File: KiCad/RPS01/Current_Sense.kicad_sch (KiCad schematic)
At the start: 8 parts, among them U7 INA139NA/250

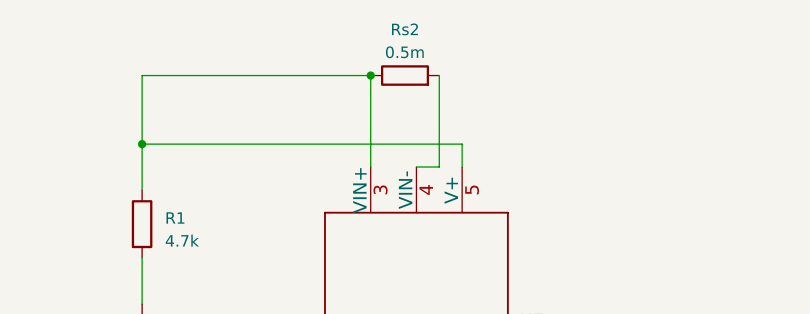
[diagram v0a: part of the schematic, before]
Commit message: 19V Update
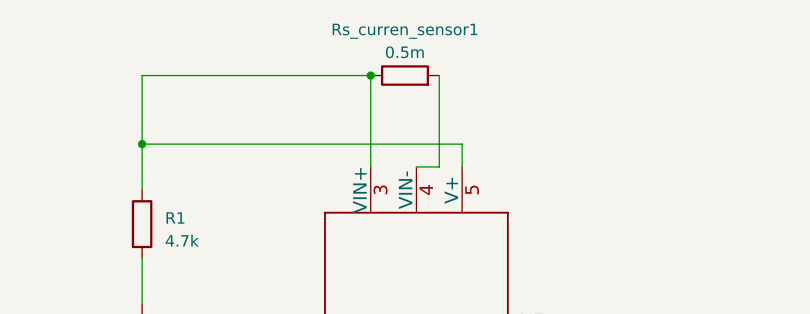
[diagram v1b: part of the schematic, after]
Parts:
- renumbered Rs2 to Rs_curren_sensor1
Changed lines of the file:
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@@
   (symbol (lib_id "Device:R") (at 62.23 38.1 90) (unit 1)
     (in_bom yes) (on_board yes) (dnp no) (fields_autoplaced)
-    (property "Reference" "Rs2" (at 62.23 33.02 90)
+    (property "Reference" "Rs_curren_sensor1" (at 62.23 33.02 90)
       (effects (font (size 1.27 1.27)))
     )
@@
       (project "rps01"
         (path "/14930f15-c0a0-4b55-93e6-b112548415f6/13e150ee-6c46-47a5-9c09-3749eb0dcbfe"
-          (reference "Rs2") (unit 1)
+          (reference "Rs_curren_sensor1") (unit 1)
         )
       )

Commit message: Deleted Current Sense Circuit to remove errors and started 5V system
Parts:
- removed C1, C2: 0.1mu, Capacitor_SMD:C_1206_3216Metric, symbol Device:C
- removed R1: 4.7k, Resistor_SMD:R_1206_3216Metric, symbol Device:R
- removed R2: 10k, Resistor_SMD:R_1206_3216Metric, symbol Device:R
- removed R3: 1k, Resistor_SMD:R_1206_3216Metric, symbol Device:R
- removed RL1: 72.3k, Resistor_SMD:R_1210_3225Metric, symbol Device:R
- removed Rs_curren_sensor1: 0.5m, Resistor_SMD:R_1206_3216Metric, symbol Device:R
- removed U7: INA139NA/250, Mechatronic Footprints:INA139_PW8, symbol 2023-04-06_06-18-16:INA139NA/250

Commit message: Add Current Sense to RPS01
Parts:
- added R1: 0.3m, symbol Device:R
- added U12: INA139QPWRQ1, PW8, symbol INA139:INA139QPWRQ1
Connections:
- new net +5V: U12.8 (V-)
- new net GND: U12.4 (GND)
- new net Load: R1.2, U12.1 (VIN-)
- new net SenseVoltage: U12.6 (OUT)
- new net Vp: R1.1, U12.2 (VIN+)
- no-connect marks 0 -> 3
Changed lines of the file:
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@@
 (kicad_sch (version 20230121) (generator eeschema)
   (paper "A4")
-  (image (at 123.19 160.528) (scale 1.22369)
+  (junction (at 104.14 35.56) (diameter 0) (color 0 0 0 0)
+  )
+  (junction (at 113.6342 35.56) (diameter 0) (color 0 0 0 0)
+  )
+  (no_connect (at 101.6 97.79))
+  (no_connect (at 104.14 41.91))
+  (no_connect (at 106.68 97.79))
+  (wire (pts (xy 105.41 35.56) (xy 104.14 35.56))
+    (stroke (width 0) (type default))
+  )
+  (wire (pts (xy 85.09 35.56) (xy 104.14 35.56))
+    (stroke (width 0) (type default))
+  )
+  (wire (pts (xy 101.6 41.91) (xy 81.28 41.91))
+    (stroke (width 0) (type default))
+  )
+  (wire (pts (xy 109.22 97.79) (xy 123.19 97.79))
+    (stroke (width 0) (type default))
+  )
+  (wire (pts (xy 113.6342 35.56) (xy 139.7 35.56))
+    (stroke (width 0) (type default))
+  )
+  (wire (pts (xy 113.6342 41.91) (xy 109.22 41.91))
+    (stroke (width 0) (type default))
+  )
+  (wire (pts (xy 104.14 97.79) (xy 104.14 101.6))
+    (stroke (width 0) (type default))
+  )
+  (wire (pts (xy 113.6342 35.56) (xy 113.6342 41.91))
+    (stroke (width 0) (type default))
+  )
+  (wire (pts (xy 113.03 35.56) (xy 113.6342 35.56))
+    (stroke (width 0) (type default))
+  )
+  (wire (pts (xy 81.28 41.91) (xy 81.28 53.34))
+    (stroke (width 0) (type default))
+  )
+  (wire (pts (xy 104.14 101.6) (xy 133.35 101.6))
+    (stroke (width 0) (type default))
+  )
+  (wire (pts (xy 104.14 38.3106) (xy 104.14 35.56))
+    (stroke (width 0) (type default))
+  )
+  (wire (pts (xy 106.68 41.91) (xy 106.68 38.3106))
+    (stroke (width 0) (type default))
+  )
+  (wire (pts (xy 106.68 38.3106) (xy 104.14 38.3106))
+    (stroke (width 0) (type default))
+  )
+  (image (at 120.65 142.748) (scale 1.22369)
     (data
       iVBORw0KGgoAAAANSUhEUgAAA2QAAAJMCAIAAAAaAvJwAAAAA3NCSVQICAjb4U/gAAAACXBIWXMA
@@
     )
   )
-  (image (at 197.612 70.358) (scale 1.93163)
+  (image (at 231.902 47.498) (scale 1.16665)
     (data
       iVBORw0KGgoAAAANSUhEUgAABAIAAAKsCAIAAAD5hIhGAAAAA3NCSVQICAjb4U/gAAAACXBIWXMA
@@
     )
   )
+  (hierarchical_label "Load" (shape input) (at 139.7 35.56 0) (fields_autoplaced)
+    (effects (font (size 1.27 1.27)) (justify left))
+  )
+  (hierarchical_label "SenseVoltage" (shape input) (at 133.35 101.6 0) (fields_autoplaced)
+    (effects (font (size 1.27 1.27)) (justify left))
+  )
+  (hierarchical_label "Vp" (shape input) (at 85.09 35.56 180) (fields_autoplaced)
+    (effects (font (size 1.27 1.27)) (justify right))
+  )
+  (symbol (lib_id "power:GND") (at 81.28 53.34 0) (unit 1)
+    (in_bom yes) (on_board yes) (dnp no) (fields_autoplaced)
+    (property "Reference" "#PWR030" (at 81.28 59.69 0)
+      (effects (font (size 1.27 1.27)) hide)
+    )
+    (property "Value" "GND" (at 81.28 58.42 0)
+      (effects (font (size 1.27 1.27)))
+    )
+    (property "Footprint" "" (at 81.28 53.34 0)
+      (effects (font (size 1.27 1.27)) hide)
+    )
+    (property "Datasheet" "" (at 81.28 53.34 0)
+      (effects (font (size 1.27 1.27)) hide)
+    )
+    (pin "1")
+    (instances
+      (project "rps01"
+        (path "/14930f15-c0a0-4b55-93e6-b112548415f6/13e150ee-6c46-47a5-9c09-3749eb0dcbfe"
+          (reference "#PWR030") (unit 1)
+        )
+      )
+    )
+  )
+  (symbol (lib_id "Device:R") (at 109.22 35.56 90) (unit 1)
+    (in_bom yes) (on_board yes) (dnp no) (fields_autoplaced)
+    (property "Reference" "R1" (at 109.22 30.48 90)
+      (effects (font (size 1.27 1.27)))
+    )
+    (property "Value" "0.3m" (at 109.22 33.02 90)
+      (effects (font (size 1.27 1.27)))
+    )
+    (property "Footprint" "" (at 109.22 37.338 90)
+      (effects (font (size 1.27 1.27)) hide)
+    )
+    (property "Datasheet" "~" (at 109.22 35.56 0)
+      (effects (font (size 1.27 1.27)) hide)
+    )
+    (pin "1")
+    (pin "2")
+    (instances
+      (project "rps01"
+        (path "/14930f15-c0a0-4b55-93e6-b112548415f6/13e150ee-6c46-47a5-9c09-3749eb0dcbfe"
+          (reference "R1") (unit 1)
+        )
+      )
+    )
+  )
+  (symbol (lib_id "power:+5V") (at 123.19 97.79 270) (unit 1)
+    (in_bom yes) (on_board yes) (dnp no) (fields_autoplaced)
+    (property "Reference" "#PWR031" (at 119.38 97.79 0)
+      (effects (font (size 1.27 1.27)) hide)
+    )
+    (property "Value" "+5V" (at 127 98.425 90)
+      (effects (font (size 1.27 1.27)) (justify left))
+    )
+    (property "Footprint" "" (at 123.19 97.79 0)
+      (effects (font (size 1.27 1.27)) hide)
+    )
+    (property "Datasheet" "" (at 123.19 97.79 0)
+      (effects (font (size 1.27 1.27)) hide)
+    )
+    (pin "1")
+    (instances
+      (project "rps01"
+        (path "/14930f15-c0a0-4b55-93e6-b112548415f6/13e150ee-6c46-47a5-9c09-3749eb0dcbfe"
+          (reference "#PWR031") (unit 1)
+        )
+      )
+    )
+  )
+  (symbol (lib_id "INA139:INA139QPWRQ1") (at 109.22 41.91 270) (unit 1)
+    (in_bom yes) (on_board yes) (dnp no) (fields_autoplaced)
+    (property "Reference" "U12" (at 115.57 69.215 90)
+      (effects (font (size 1.524 1.524)) (justify left))
+    )
+    (property "Value" "INA139QPWRQ1" (at 115.57 71.755 90)
+      (effects (font (size 1.524 1.524)) (justify left))
+    )
+    (property "Footprint" "PW8" (at 109.22 41.91 0)
+      (effects (font (size 1.27 1.27) italic) hide)
+    )
+    (property "Datasheet" "INA139QPWRQ1" (at 109.22 41.91 0)
+      (effects (font (size 1.27 1.27) italic) hide)
+    )
+    (pin "1")
+    (pin "2")
+    (pin "3")
+    (pin "4")
+    (pin "5")
+    (pin "6")
+    (pin "7")
+    (pin "8")
+    (instances
+      (project "rps01"
+        (path "/14930f15-c0a0-4b55-93e6-b112548415f6/13e150ee-6c46-47a5-9c09-3749eb0dcbfe"
+          (reference "U12") (unit 1)
+        )
+      )
+    )
+  )

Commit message: Add Fuses and other ADC pin
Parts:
- R1: footprint (none) -> Mechatronic Footprints:CSS2H-5930R
- U12: footprint PW8 -> Mechatronic Footprints:INA139_PW8
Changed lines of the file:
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@@
       (effects (font (size 1.27 1.27)))
     )
-    (property "Footprint" "" (at 109.22 37.338 90)
+    (property "Footprint" "Mechatronic Footprints:CSS2H-5930R" (at 109.22 37.338 90)
       (effects (font (size 1.27 1.27)) hide)
     )
@@
       (effects (font (size 1.524 1.524)) (justify left))
     )
-    (property "Footprint" "PW8" (at 109.22 41.91 0)
+    (property "Footprint" "Mechatronic Footprints:INA139_PW8" (at 109.22 41.91 0)
       (effects (font (size 1.27 1.27) italic) hide)
     )

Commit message: adjustments to main board revision
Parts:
- added Cf_1: 80pF, symbol Device:C
- added RL: 100k, symbol Device:R
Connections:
- net GND: now also Cf_1.2, RL.1
- net SenseVoltage: now also Cf_1.1, RL.2
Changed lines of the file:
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@@
   (junction (at 104.14 35.56) (diameter 0) (color 0 0 0 0)
   )
+  (junction (at 111.76 117.3986) (diameter 0) (color 0 0 0 0)
+  )
   (junction (at 113.6342 35.56) (diameter 0) (color 0 0 0 0)
   )
+  (junction (at 121.92 101.6158) (diameter 0) (color 0 0 0 0)
+  )
+  (junction (at 111.76 101.6158) (diameter 0) (color 0 0 0 0)
+  )
   (no_connect (at 101.6 97.79))
   (no_connect (at 104.14 41.91))
   (no_connect (at 106.68 97.79))
+  (wire (pts (xy 121.92 101.6158) (xy 133.35 101.6158))
+    (stroke (width 0) (type default))
+  )
   (wire (pts (xy 105.41 35.56) (xy 104.14 35.56))
     (stroke (width 0) (type default))
   )
+  (wire (pts (xy 121.92 113.03) (xy 121.92 117.3986))
+    (stroke (width 0) (type default))
+  )
+  (wire (pts (xy 111.76 101.6158) (xy 111.76 105.41))
+    (stroke (width 0) (type default))
+  )
   (wire (pts (xy 85.09 35.56) (xy 104.14 35.56))
     (stroke (width 0) (type default))
   )
+  (wire (pts (xy 121.92 117.3986) (xy 111.76 117.3986))
+    (stroke (width 0) (type default))
+  )
   (wire (pts (xy 101.6 41.91) (xy 81.28 41.91))
     (stroke (width 0) (type default))
   )
+  (wire (pts (xy 111.76 117.3986) (xy 111.76 119.38))
+    (stroke (width 0) (type default))
+  )
   (wire (pts (xy 109.22 97.79) (xy 123.19 97.79))
     (stroke (width 0) (type default))
   )
+  (wire (pts (xy 111.76 101.6158) (xy 121.92 101.6158))
+    (stroke (width 0) (type default))
+  )
+  (wire (pts (xy 111.76 101.6) (xy 111.76 101.6158))
+    (stroke (width 0) (type default))
+  )
   (wire (pts (xy 113.6342 35.56) (xy 139.7 35.56))
     (stroke (width 0) (type default))
   )
+  (wire (pts (xy 133.35 101.6158) (xy 133.35 101.6))
+    (stroke (width 0) (type default))
+  )
   (wire (pts (xy 113.6342 41.91) (xy 109.22 41.91))
     (stroke (width 0) (type default))
@@
     (stroke (width 0) (type default))
   )
-  (wire (pts (xy 104.14 101.6) (xy 133.35 101.6))
-    (stroke (width 0) (type default))
-  )
   (wire (pts (xy 104.14 38.3106) (xy 104.14 35.56))
     (stroke (width 0) (type default))
@@
     (stroke (width 0) (type default))
   )
-  (image (at 120.65 142.748) (scale 1.22369)
+  (wire (pts (xy 111.76 113.03) (xy 111.76 117.3986))
+    (stroke (width 0) (type default))
+  )
+  (wire (pts (xy 104.14 101.6) (xy 111.76 101.6))
+    (stroke (width 0) (type default))
+  )
+  (wire (pts (xy 121.92 101.6158) (xy 121.92 105.41))
+    (stroke (width 0) (type default))
+  )
+  (image (at 190.2968 139.2682) (scale 1.22369)
     (data
       iVBORw0KGgoAAAANSUhEUgAAA2QAAAJMCAIAAAAaAvJwAAAAA3NCSVQICAjb4U/gAAAACXBIWXMA
@@
     )
   )
+  (symbol (lib_id "Device:C") (at 121.92 109.22 0) (unit 1)
+    (in_bom yes) (on_board yes) (dnp no) (fields_autoplaced)
+    (property "Reference" "Cf_1" (at 125.73 108.585 0)
+      (effects (font (size 1.27 1.27)) (justify left))
+    )
+    (property "Value" "80pF" (at 125.73 111.125 0)
+      (effects (font (size 1.27 1.27)) (justify left))
+    )
+    (property "Footprint" "" (at 122.8852 113.03 0)
+      (effects (font (size 1.27 1.27)) hide)
+    )
+    (property "Datasheet" "~" (at 121.92 109.22 0)
+      (effects (font (size 1.27 1.27)) hide)
+    )
+    (pin "1")
+    (pin "2")
+    (instances
+      (project "rps01"
+        (path "/14930f15-c0a0-4b55-93e6-b112548415f6/13e150ee-6c46-47a5-9c09-3749eb0dcbfe"
+          (reference "Cf_1") (unit 1)
+        )
+      )
+    )
+  )
   (symbol (lib_id "power:+5V") (at 123.19 97.79 270) (unit 1)
     (in_bom yes) (on_board yes) (dnp no) (fields_autoplaced)
@@
     )
   )
+  (symbol (lib_id "power:GND") (at 111.76 119.38 0) (unit 1)
+    (in_bom yes) (on_board yes) (dnp no) (fields_autoplaced)
+    (property "Reference" "#PWR040" (at 111.76 125.73 0)
+      (effects (font (size 1.27 1.27)) hide)
+    )
+    (property "Value" "GND" (at 111.76 124.6124 0)
+      (effects (font (size 1.27 1.27)))
+    )
+    (property "Footprint" "" (at 111.76 119.38 0)
+      (effects (font (size 1.27 1.27)) hide)
+    )
+    (property "Datasheet" "" (at 111.76 119.38 0)
+      (effects (font (size 1.27 1.27)) hide)
+    )
+    (pin "1")
+    (instances
+      (project "rps01"
+        (path "/14930f15-c0a0-4b55-93e6-b112548415f6/13e150ee-6c46-47a5-9c09-3749eb0dcbfe"
+          (reference "#PWR040") (unit 1)
+        )
+      )
+    )
+  )
   (symbol (lib_id "INA139:INA139QPWRQ1") (at 109.22 41.91 270) (unit 1)
     (in_bom yes) (on_board yes) (dnp no) (fields_autoplaced)
@@
         )
       )
+    )
+  )
+  (symbol (lib_id "Device:R") (at 111.76 109.22 180) (unit 1)
+    (in_bom yes) (on_board yes) (dnp no) (fields_autoplaced)
+    (property "Reference" "RL" (at 114.3 108.585 0)
+      (effects (font (size 1.27 1.27)) (justify right))
+    )
+    (property "Value" "100k" (at 114.3 111.125 0)
+      (effects (font (size 1.27 1.27)) (justify right))
+    )
+    (property "Footprint" "" (at 113.538 109.22 90)
+      (effects (font (size 1.27 1.27)) hide)
+    )
+    (property "Datasheet" "~" (at 111.76 109.22 0)
+      (effects (font (size 1.27 1.27)) hide)
+    )
+    (pin "1")
+    (pin "2")
+    (instances
+      (project "rps01"
+        (path "/14930f15-c0a0-4b55-93e6-b112548415f6/13e150ee-6c46-47a5-9c09-3749eb0dcbfe"
+          (reference "RL") (unit 1)
+        )
+      )

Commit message: Updated Layout
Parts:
- renumbered RL to RL1
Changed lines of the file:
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@@
   (symbol (lib_id "Device:R") (at 111.76 109.22 180) (unit 1)
     (in_bom yes) (on_board yes) (dnp no) (fields_autoplaced)
-    (property "Reference" "RL" (at 114.3 108.585 0)
+    (property "Reference" "RL1" (at 114.3 108.585 0)
       (effects (font (size 1.27 1.27)) (justify right))
     )
@@
       (project "rps01"
         (path "/14930f15-c0a0-4b55-93e6-b112548415f6/13e150ee-6c46-47a5-9c09-3749eb0dcbfe"
-          (reference "RL") (unit 1)
+          (reference "RL1") (unit 1)
         )
       )

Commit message: updates
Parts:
- Cf_1: footprint (none) -> Capacitor_SMD:C_0603_1608Metric
- RL1: footprint (none) -> Resistor_SMD:R_0603_1608Metric
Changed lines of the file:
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@@
       (effects (font (size 1.27 1.27)) (justify left))
     )
-    (property "Footprint" "" (at 122.8852 113.03 0)
+    (property "Footprint" "Capacitor_SMD:C_0603_1608Metric" (at 122.8852 113.03 0)
       (effects (font (size 1.27 1.27)) hide)
     )
@@
       (effects (font (size 1.27 1.27)) (justify right))
     )
-    (property "Footprint" "" (at 113.538 109.22 90)
+    (property "Footprint" "Resistor_SMD:R_0603_1608Metric" (at 113.538 109.22 90)
       (effects (font (size 1.27 1.27)) hide)
     )

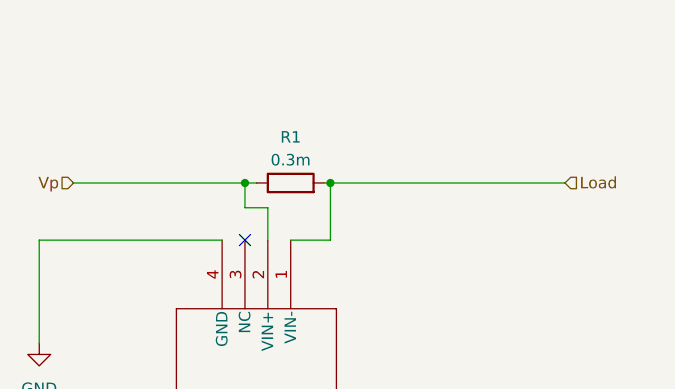
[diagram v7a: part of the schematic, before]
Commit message: updated shunt resistor
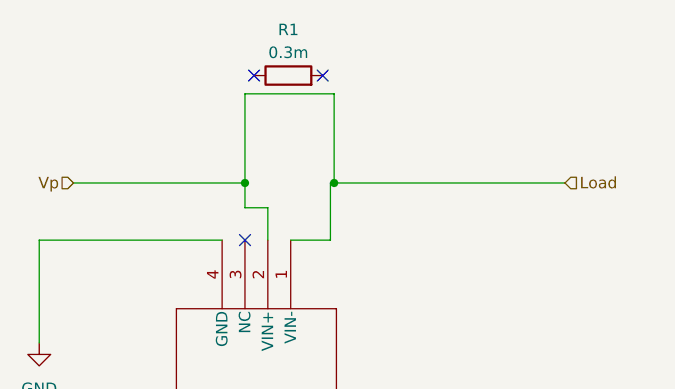
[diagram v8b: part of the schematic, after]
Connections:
- net Load: now also U12.2 (VIN+); no longer R1.2
- net Vp: no longer names the net of R1.1
- net Vp: no longer U12.2 (VIN+)
- no-connect marks 3 -> 5
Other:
- moved on the sheet: R1
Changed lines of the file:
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@@
   (junction (at 111.76 117.3986) (diameter 0) (color 0 0 0 0)
   )
-  (junction (at 113.6342 35.56) (diameter 0) (color 0 0 0 0)
+  (junction (at 114.046 35.56) (diameter 0) (color 0 0 0 0)
   )
   (junction (at 121.92 101.6158) (diameter 0) (color 0 0 0 0)
@@
   (junction (at 111.76 101.6158) (diameter 0) (color 0 0 0 0)
   )
+  (no_connect (at 105.156 23.622))
   (no_connect (at 101.6 97.79))
+  (no_connect (at 112.776 23.622))
   (no_connect (at 104.14 41.91))
   (no_connect (at 106.68 97.79))
@@
     (stroke (width 0) (type default))
   )
-  (wire (pts (xy 105.41 35.56) (xy 104.14 35.56))
-    (stroke (width 0) (type default))
-  )
   (wire (pts (xy 121.92 113.03) (xy 121.92 117.3986))
     (stroke (width 0) (type default))
@@
     (stroke (width 0) (type default))
   )
+  (wire (pts (xy 114.046 25.654) (xy 114.046 35.56))
+    (stroke (width 0) (type default))
+  )
   (wire (pts (xy 101.6 41.91) (xy 81.28 41.91))
     (stroke (width 0) (type default))
@@
     (stroke (width 0) (type default))
   )
+  (wire (pts (xy 104.14 35.56) (xy 104.14 25.654))
+    (stroke (width 0) (type default))
+  )
   (wire (pts (xy 109.22 97.79) (xy 123.19 97.79))
     (stroke (width 0) (type default))
@@
     (stroke (width 0) (type default))
   )
-  (wire (pts (xy 113.6342 35.56) (xy 139.7 35.56))
+  (wire (pts (xy 113.6342 35.56) (xy 114.046 35.56))
     (stroke (width 0) (type default))
   )
@@
     (stroke (width 0) (type default))
   )
-  (wire (pts (xy 104.14 97.79) (xy 104.14 101.6))
+  (wire (pts (xy 104.14 25.654) (xy 114.046 25.654))
     (stroke (width 0) (type default))
   )
-  (wire (pts (xy 113.6342 35.56) (xy 113.6342 41.91))
+  (wire (pts (xy 104.14 97.79) (xy 104.14 101.6))
     (stroke (width 0) (type default))
   )
-  (wire (pts (xy 113.03 35.56) (xy 113.6342 35.56))
+  (wire (pts (xy 113.6342 35.56) (xy 113.6342 41.91))
     (stroke (width 0) (type default))
   )
@@
     (stroke (width 0) (type default))
   )
+  (wire (pts (xy 114.046 35.56) (xy 139.7 35.56))
+    (stroke (width 0) (type default))
+  )
   (wire (pts (xy 104.14 101.6) (xy 111.76 101.6))
     (stroke (width 0) (type default))
@@
     )
   )
-  (symbol (lib_id "Device:R") (at 109.22 35.56 90) (unit 1)
+  (symbol (lib_id "Device:R") (at 108.966 23.622 90) (unit 1)
     (in_bom yes) (on_board yes) (dnp no) (fields_autoplaced)
-    (property "Reference" "R1" (at 109.22 30.48 90)
+    (property "Reference" "R1" (at 108.966 18.542 90)
       (effects (font (size 1.27 1.27)))
     )
-    (property "Value" "0.3m" (at 109.22 33.02 90)
+    (property "Value" "0.3m" (at 108.966 21.082 90)
       (effects (font (size 1.27 1.27)))
     )
-    (property "Footprint" "Mechatronic Footprints:CSS2H-5930R" (at 109.22 37.338 90)
+    (property "Footprint" "Mechatronic Footprints:CSS2H-5930R" (at 108.966 25.4 90)
       (effects (font (size 1.27 1.27)) hide)
     )
-    (property "Datasheet" "~" (at 109.22 35.56 0)
+    (property "Datasheet" "~" (at 108.966 23.622 0)
       (effects (font (size 1.27 1.27)) hide)
     )
